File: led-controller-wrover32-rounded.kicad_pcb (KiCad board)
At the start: 4 copper layers, 36 x 40 mm, 138 parts, among them J101 Molex PicoBlade 4-pin, J102 Molex PicoBlade 6-pin, J103 PicoBlade 3 pin, J104 USB_B_Micro, J105 POWER IN, J106 Molex PicoBlade 6-pin, J107 Conn_01x09_MountingPin, J108 12V_OUT, J109 Micro_SD_Card, J110 Molex PicoBlade 4-pin, J111 Fan PWM, J112 GPIO_CONN, Q101 UMH3N, Q102 BSS138PW,115, Q103 IRFHS9351, Q104 BSS138PW,115, SW101 KMR2, SW102 KMR2, U101 TPS2001DDBVX, U102 USBUF02W6, U103 NTS0104BQ,115, U104 TPS61089RNRR, U105 MPM3810GQB-33, U106 SSM2518CPZ, U107 ESP32-S3-WROOM-2-N32R8, U108 SN74AUP1G08YZP, U109 BME280, U110 BNO086, U111 SX1509BIULTRT, Y101 OM-7604-C7

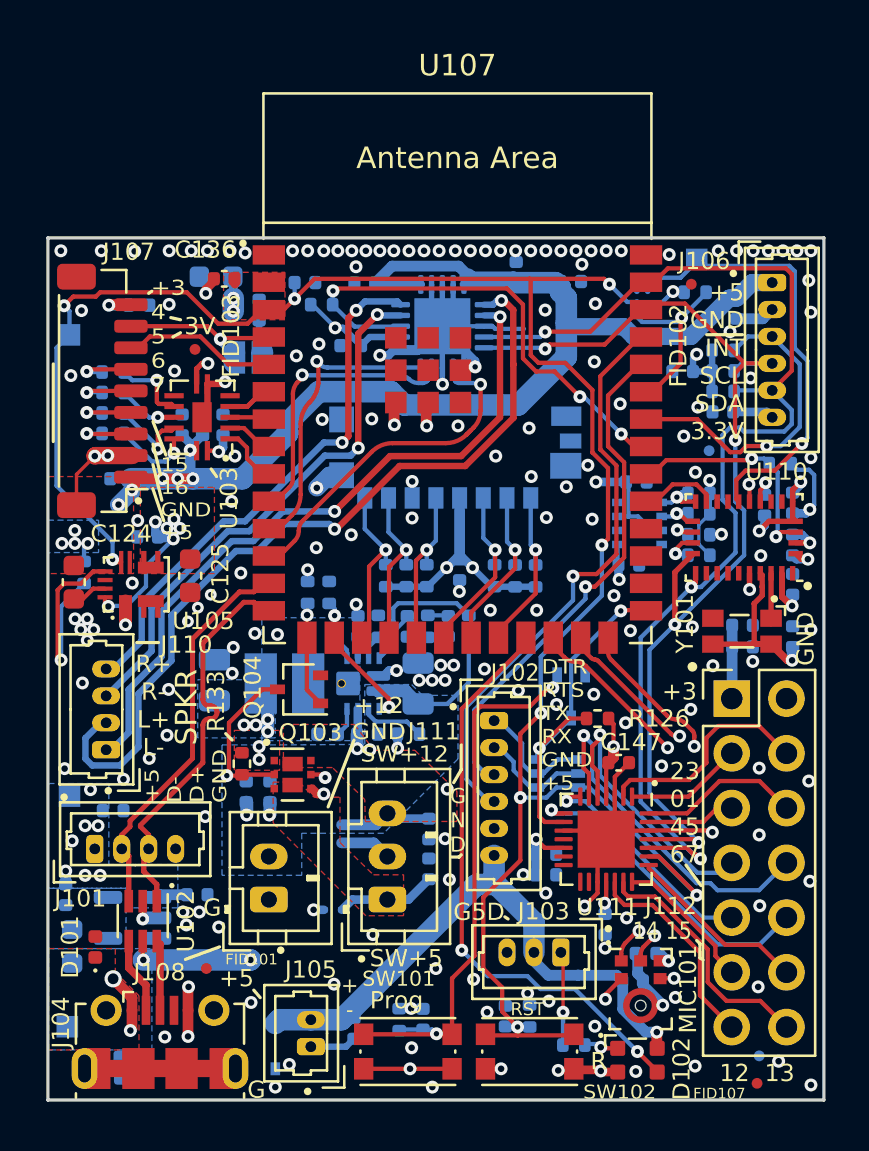
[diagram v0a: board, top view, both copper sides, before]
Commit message: Moved to ESP32 S3 Wroom 1
The Wroom 2 requires 1.8V on a couple of GPIOs.  Since I don't need 32MB of
flash the Wroom 1 is used instead.  The footprint is slightly different,
however.

Signed-off-by: Aaron Williams <aaron.w2@gmail.com>
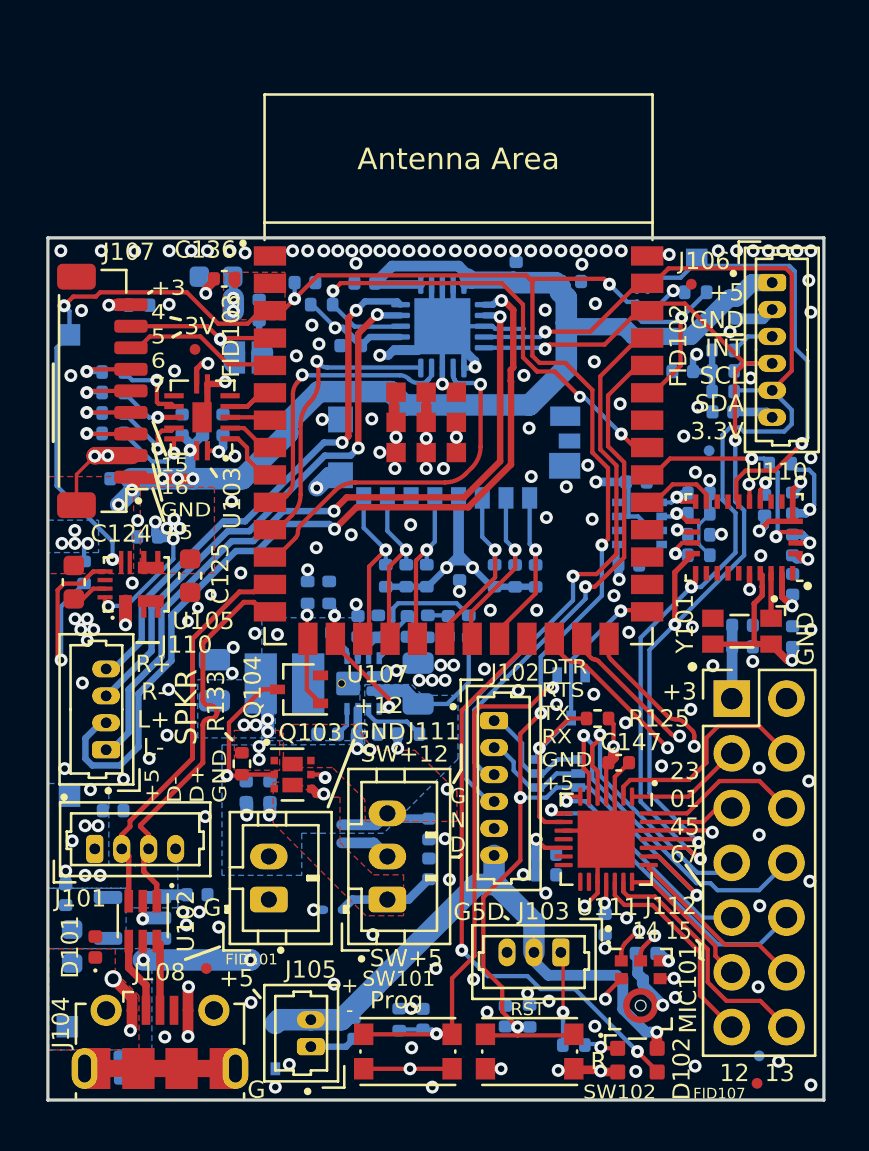
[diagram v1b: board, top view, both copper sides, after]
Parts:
- U107: value ESP32-S3-WROOM-2-N32R8 -> ESP32-S3-WROOM-1; footprint Espressif:ESP32-S3-WROOM-2 -> Espressif:ESP32-S3-WROOM-1
- moved U107 0.07 mm to (79.0, 39.1)
- renumbered R126 to R125, R125 to R126
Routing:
- net INT3: track 15.0 -> 2.03 mm, vias 1 -> 0
- net /Reset, Boot, Amp, and SD Card/SPKR_L-: track 32.2 -> 33.5 mm
- net /Reset, Boot, Amp, and SD Card/SPKR_L+: track 38.1 -> 39.3 mm
- net +3V3: track 91.0 -> 92.0 mm
- net GND: track 72.4 -> 72.3 mm, vias 186 -> 190

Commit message: Changed ESP32 to ESP32-S3-WROOM-1 and other cleanup
Signed-off-by: Aaron Williams <aaron.w2@gmail.com>
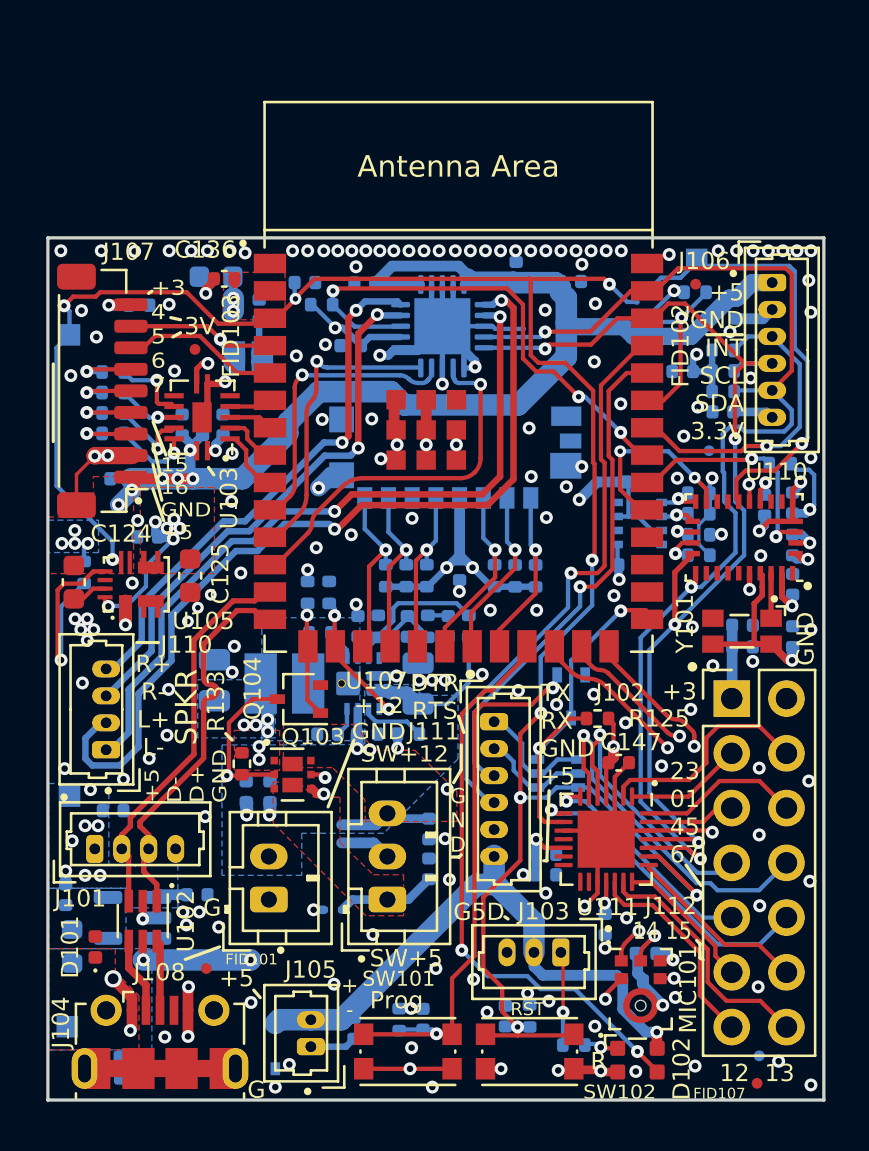
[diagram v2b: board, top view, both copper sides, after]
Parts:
- moved Q104 0.45 mm to (71.7, 51.4)
- moved U107 0.35 mm to (79.0, 39.5)
- moved FID102 0.20 mm to (90.0, 32.1)
- moved J102 0.05 mm to (80.7, 52.5)
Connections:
- J106 pad 3: INT3 -> ~{INT3}
- R107 pad 1: INT3 -> ~{INT3}
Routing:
- net ~{INT3}: track 0.00 -> 14.3 mm, vias 0 -> 1
- net ~{INT2}: track 3.20 -> 8.42 mm, vias 0 -> 2
- net INT3: track 2.03 -> 0.00 mm
- net IO6: track 3.51 -> 1.56 mm
- net ~{RST_BNO085}: track 7.84 -> 9.00 mm
- net SD_CMD: track 7.75 -> 8.78 mm
- net RXD0: track 26.5 -> 25.8 mm
- net SDA: track 54.6 -> 55.3 mm
- net I2S1_WSEL: track 12.4 -> 12.9 mm
- net /Reset, Boot, Amp, and SD Card/SPKR_L+: track 39.3 -> 39.9 mm
- net ~{RESET}: track 101.6 -> 101.1 mm
- net GND: track 72.3 -> 72.2 mm, vias 190 -> 180
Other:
- board text added: "DTR RTS"
- board text added: "TX RX GND +5"
- board text removed: "DTR RTS TX RX GND +5"

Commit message: Fixed ESP32 footprint
Apparently the footprint changed so this reflects the latest update.

Signed-off-by: Aaron Williams <aaron.w2@gmail.com>
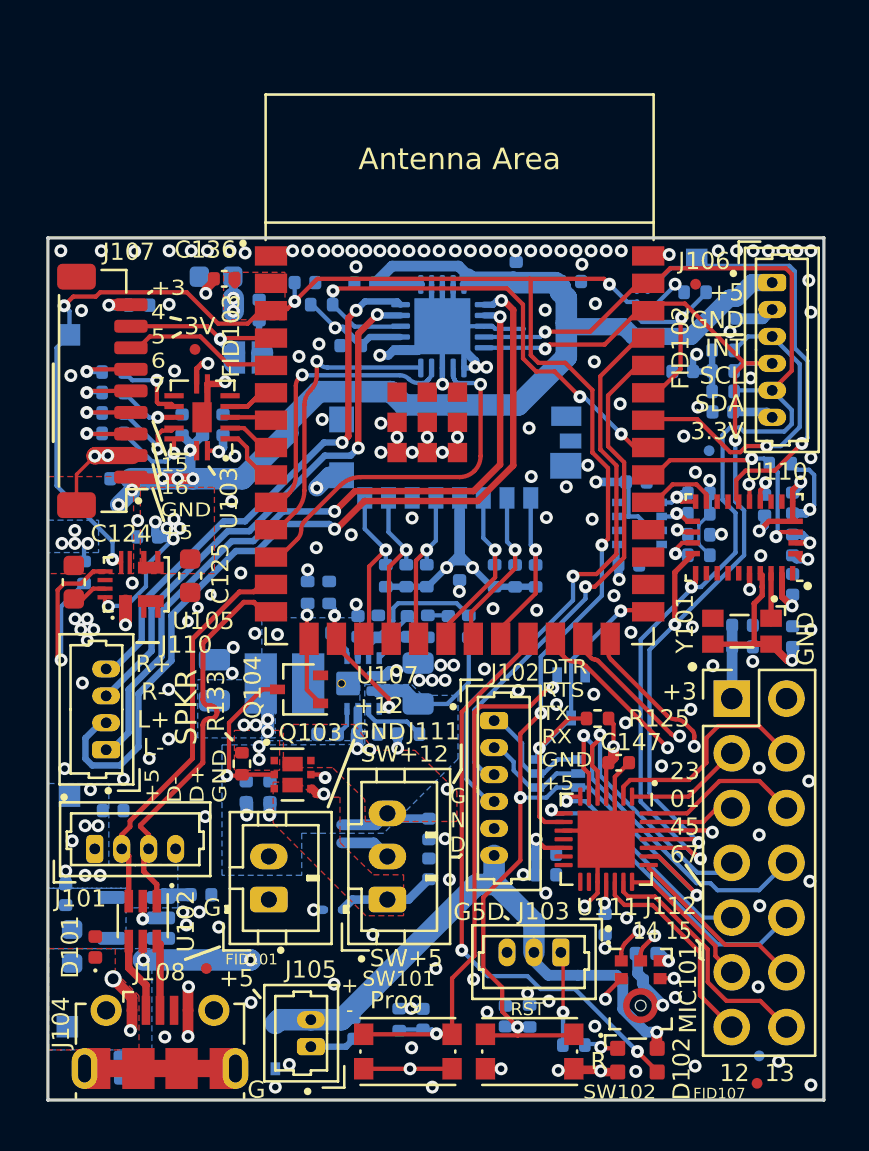
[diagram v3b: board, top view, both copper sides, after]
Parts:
- D102: value WS2812_2020 -> WS2812_2020C
- moved Q104 0.45 mm to (71.7, 51.0)
- moved U107 0.35 mm to (79.1, 39.1)
- moved C103 0.17 mm to (67.1, 60.5)
- moved U101 0.17 mm to (64.1, 61.5)
- moved J102 0.05 mm to (80.7, 52.4)
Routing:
- net ~{INT2}: track 8.42 -> 3.20 mm, vias 2 -> 0
- net IO6: track 1.56 -> 3.51 mm
- net GND: track 72.2 -> 70.5 mm, vias 180 -> 188
- net SD_CMD: track 8.78 -> 7.73 mm
- net RXD0: track 25.8 -> 26.8 mm
- net ~{RST_BNO085}: track 9.00 -> 8.20 mm
- net SDA: track 55.3 -> 54.6 mm
- net ~{INT3}: track 14.3 -> 15.0 mm
- net I2S0_BCLK: track 18.0 -> 18.6 mm
- net AMP_PWR: track 23.3 -> 22.7 mm
- net ~{RESET}: track 101.1 -> 101.6 mm
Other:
- board text added: "DTR RTS TX RX GND +5"
- board text added: "S +5 G"
- board text removed: "DTR RTS"
- board text removed: "G +5 S"
- board text removed: "TX RX GND +5"
